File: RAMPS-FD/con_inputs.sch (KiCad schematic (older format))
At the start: 7 parts, among them P801 ENDSTOPS, P802 - X + - Y + - Z +, U801 4050_RMC

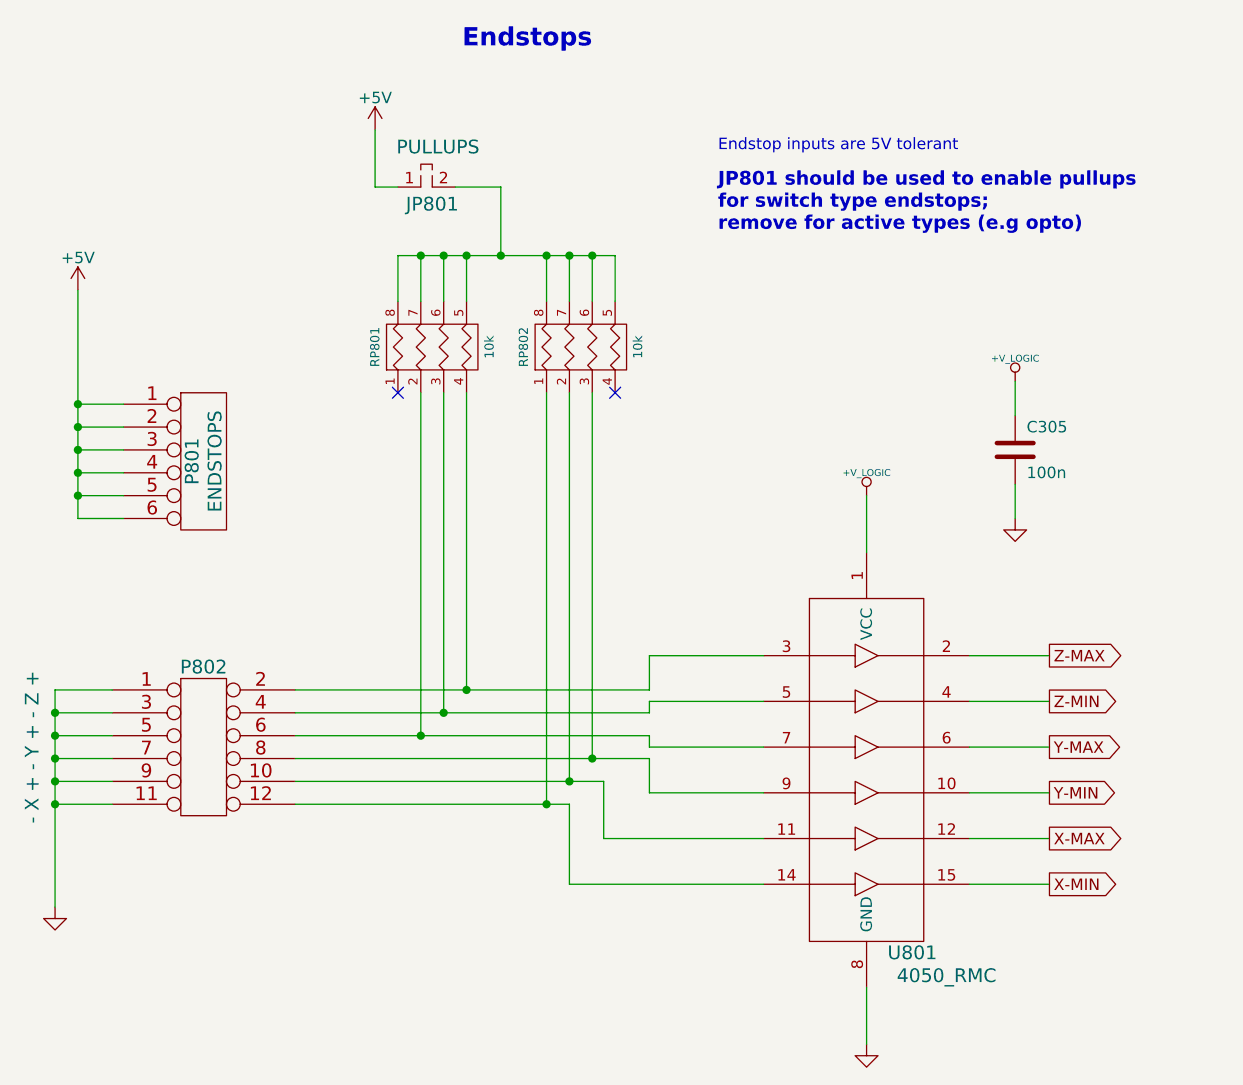
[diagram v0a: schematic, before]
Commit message: Changed fuse holders to Keystone 3568; specificy HCT instead of ACT logic
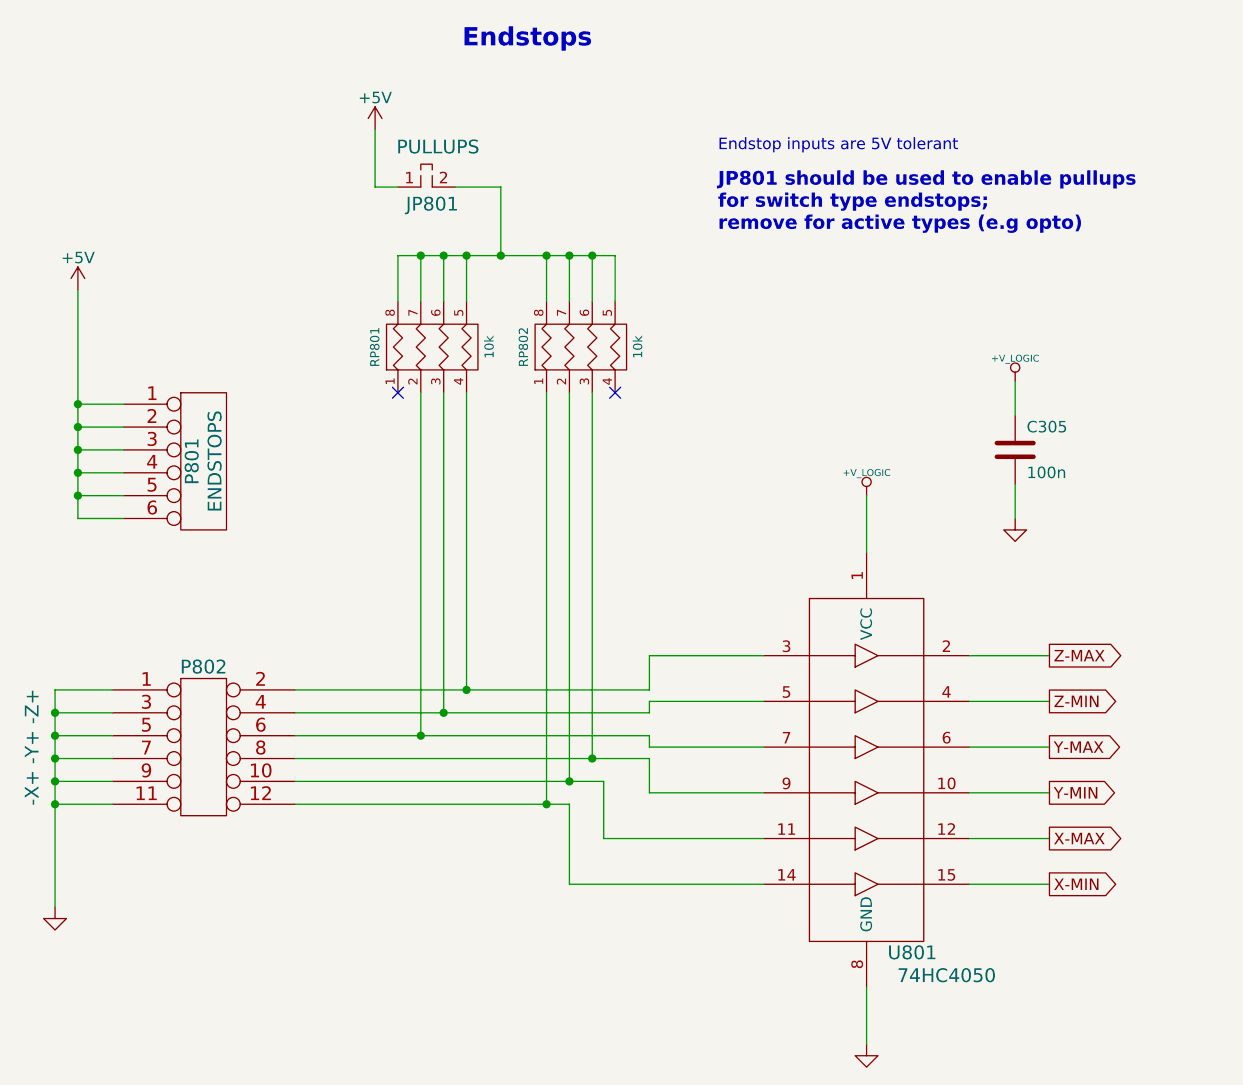
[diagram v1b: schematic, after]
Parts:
- JP801: footprint pin_array:PIN_ARRAY_2X1 -> Pin_Headers:Pin_Header_Straight_1x02
- P801: footprint w_pin_strip:pin_strip_6 -> Pin_Headers:Pin_Header_Straight_1x06
- P802: value - X + - Y + - Z + -> -X+ -Y+ -Z+; footprint w_pin_strip:pin_strip_6x2 -> Pin_Headers:Pin_Header_Straight_2x06
- U801: value 4050_RMC -> 74HC4050
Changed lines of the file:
@@
 P 4450 3150
 F 0 "U801" H 4450 1600 60  0000 C CNN
-F 1 "4050_RMC" H 4600 1500 60  0000 C CNN
+F 1 "74HC4050" H 4600 1500 60  0000 C CNN
 F 2 "Housings_SSOP:TSSOP-16_4.4x5mm_Pitch0.65mm" H 4450 3150 60  0001 C CNN
 F 3 "~" H 4450 3150 60  0000 C CNN
@@
 F 0 "JP801" H 2350 1275 60  0000 C CNN
 F 1 "PULLUPS" H 2375 1525 60  0000 C CNN
-F 2 "pin_array:PIN_ARRAY_2X1" H 2350 1350 60  0001 C CNN
+F 2 "Pin_Headers:Pin_Header_Straight_1x02" H 2350 1350 60  0001 C CNN
 F 3 "~" H 2350 1350 60  0000 C CNN
 	1    2350 1350
@@
 P 1350 3800
 F 0 "P802" H 1350 4150 60  0000 C CNN
-F 1 "- X + - Y + - Z +" V 600 3800 60  0000 C CNN
-F 2 "w_pin_strip:pin_strip_6x2" H 1350 3800 60  0001 C CNN
+F 1 "-X+ -Y+ -Z+" V 600 3800 60  0000 C CNN
+F 2 "Pin_Headers:Pin_Header_Straight_2x06" H 1350 3800 60  0001 C CNN
 F 3 "" H 1350 3800 60  0000 C CNN
 	1    1350 3800
@@
 F 0 "P801" V 1300 2550 60  0000 C CNN
 F 1 "ENDSTOPS" V 1400 2550 60  0000 C CNN
-F 2 "w_pin_strip:pin_strip_6" H 1350 2550 60  0001 C CNN
+F 2 "Pin_Headers:Pin_Header_Straight_1x06" H 1350 2550 60  0001 C CNN
 F 3 "" H 1350 2550 60  0000 C CNN
 	1    1350 2550

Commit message: Fix 3d view; remove faulty ADC protection
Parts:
- JP801: footprint Pin_Headers:Pin_Header_Straight_1x02 -> Pin_Headers:Pin_Header_Straight_1x02_Pitch2.54mm
- P801: footprint Pin_Headers:Pin_Header_Straight_1x06 -> Pin_Headers:Pin_Header_Straight_1x06_Pitch2.54mm
- P802: footprint Pin_Headers:Pin_Header_Straight_2x06 -> Pin_Headers:Pin_Header_Straight_2x06_Pitch2.54mm
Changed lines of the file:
@@
 	1750 3750 3300 3750
 $Comp
-L +V_LOGIC #PWR0105
+L +V_LOGIC #PWR0103
 U 1 1 517866F1
 P 4250 2700
-F 0 "#PWR0105" H 4250 2670 30  0001 C CNN
+F 0 "#PWR0103" H 4250 2670 30  0001 C CNN
 F 1 "+V_LOGIC" H 4250 2800 30  0000 C CNN
 F 2 "" H 4250 2700 60  0001 C CNN
@@
 $EndComp
 $Comp
-L +V_LOGIC #PWR0106
+L +V_LOGIC #PWR0104
 U 1 1 517866E5
 P 4900 2200
-F 0 "#PWR0106" H 4900 2170 30  0001 C CNN
+F 0 "#PWR0104" H 4900 2170 30  0001 C CNN
 F 1 "+V_LOGIC" H 4900 2300 30  0000 C CNN
 F 2 "" H 4900 2200 60  0001 C CNN
@@
 P 4900 2800
 AR Path="/510D87E0" Ref="#PWR0106"  Part="1"
-AR Path="/50FC37D4/510D87E0" Ref="#PWR0107"  Part="1"
-F 0 "#PWR0107" H 4900 2800 30  0001 C CNN
+AR Path="/50FC37D4/510D87E0" Ref="#PWR0105"  Part="1"
+F 0 "#PWR0105" H 4900 2800 30  0001 C CNN
 F 1 "GND" H 4900 2730 30  0001 C CNN
 F 2 "" H 4900 2800 60  0001 C CNN
@@
 $EndComp
 $Comp
-L +5V #PWR0108
+L +5V #PWR0106
 U 1 1 50FF1A76
 P 800 1800
-F 0 "#PWR0108" H 800 1650 50  0001 C CNN
+F 0 "#PWR0106" H 800 1650 50  0001 C CNN
 F 1 "+5V" H 800 1940 50  0000 C CNN
 F 2 "" H 800 1800 50  0000 C CNN
@@
 P 4250 5100
 AR Path="/50FF1A09" Ref="#PWR0108"  Part="1"
-AR Path="/50FC37D4/50FF1A09" Ref="#PWR0109"  Part="1"
-F 0 "#PWR0109" H 4250 5100 30  0001 C CNN
+AR Path="/50FC37D4/50FF1A09" Ref="#PWR0107"  Part="1"
+F 0 "#PWR0107" H 4250 5100 30  0001 C CNN
 F 1 "GND" H 4250 5030 30  0001 C CNN
 F 2 "" H 4250 5100 60  0001 C CNN
@@
 P 700 4500
 AR Path="/50FC388F" Ref="#PWR0109"  Part="1"
-AR Path="/50FC37D4/50FC388F" Ref="#PWR0110"  Part="1"
-F 0 "#PWR0110" H 700 4500 30  0001 C CNN
+AR Path="/50FC37D4/50FC388F" Ref="#PWR0108"  Part="1"
+F 0 "#PWR0108" H 700 4500 30  0001 C CNN
 F 1 "GND" H 700 4430 30  0001 C CNN
 F 2 "" H 700 4500 60  0001 C CNN
@@
 NoConn ~ 2200 2250
 $Comp
-L +5V #PWR0111
+L +5V #PWR0109
 U 1 1 524E05B1
 P 2100 1100
-F 0 "#PWR0111" H 2100 950 50  0001 C CNN
+F 0 "#PWR0109" H 2100 950 50  0001 C CNN
 F 1 "+5V" H 2100 1240 50  0000 C CNN
 F 2 "" H 2100 1100 50  0000 C CNN
@@
 F 0 "JP801" H 2350 1275 60  0000 C CNN
 F 1 "PULLUPS" H 2375 1525 60  0000 C CNN
-F 2 "Pin_Headers:Pin_Header_Straight_1x02" H 2350 1350 60  0001 C CNN
+F 2 "Pin_Headers:Pin_Header_Straight_1x02_Pitch2.54mm" H 2350 1350 60  0001 C CNN
 F 3 "~" H 2350 1350 60  0000 C CNN
 	1    2350 1350
@@
 F 0 "P802" H 1350 4150 60  0000 C CNN
 F 1 "-X+ -Y+ -Z+" V 600 3800 60  0000 C CNN
-F 2 "Pin_Headers:Pin_Header_Straight_2x06" H 1350 3800 60  0001 C CNN
+F 2 "Pin_Headers:Pin_Header_Straight_2x06_Pitch2.54mm" H 1350 3800 60  0001 C CNN
 F 3 "" H 1350 3800 60  0000 C CNN
 	1    1350 3800
@@
 F 0 "P801" V 1300 2550 60  0000 C CNN
 F 1 "ENDSTOPS" V 1400 2550 60  0000 C CNN
-F 2 "Pin_Headers:Pin_Header_Straight_1x06" H 1350 2550 60  0001 C CNN
+F 2 "Pin_Headers:Pin_Header_Straight_1x06_Pitch2.54mm" H 1350 2550 60  0001 C CNN
 F 3 "" H 1350 2550 60  0000 C CNN
 	1    1350 2550
